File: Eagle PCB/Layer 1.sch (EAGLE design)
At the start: 247 parts, among them M1C1 33nF, M1C2 680uF, M1C3 1.0uF, M1D1 RED, M1D2 BLUE, M1J1 XT30PB-F, M1Q1 AOD482, M1R1 1k, M1R10 1k, M1R11 10k, M1R12 4.7k, M1R2 1k, M1R3 3.3k, M1R4 3.3k, M1R5 1k, M1R6 1k, M1R7 1k, M1R8 10k, M1R9 10k, M2C1 33nF, M2C2 680uF, M2C3 1.0uF, M2D1 RED, M2D2 BLUE, M2J1 XT30PB-F, M2Q1 AOD482, M2R1 1k, M2R10 1k, M2R11 10k, M2R12 4.7k, M2R2 1k, M2R3 3.3k, M2R4 3.3k, M2R5 1k, M2R6 1k, M2R7 1k, M2R8 10k, M2R9 10k, M3C1 33nF, M3C2 680uF, M3C3 1.0uF, M3D1 RED, M3D2 BLUE, M3J1 XT30PB-F, M3Q1 AOD482, M3R1 1k, M3R10 1k, M3R11 10k, M3R12 4.7k, M3R2 1k, M3R3 3.3k, M3R4 3.3k, M3R5 1k, M3R6 1k, M3R7 1k, M3R8 10k, M3R9 10k, M4C1 33nF, M4C2 680uF, M4C3 1.0uF, M4D1 RED, M4D2 BLUE, M4J1 XT30PB-F, M4Q1 AOD482, M4R1 1k, M4R10 1k, M4R11 10k, M4R12 4.7k, M4R2 1k, M4R3 3.3k, M4R4 3.3k, M4R5 1k, M4R6 1k, M4R7 1k, M4R8 10k, M4R9 10k, Q1 LIGHT_SENSORALS, Q10 LIGHT_SENSORALS, Q11 LIGHT_SENSORALS, Q12 LIGHT_SENSORALS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

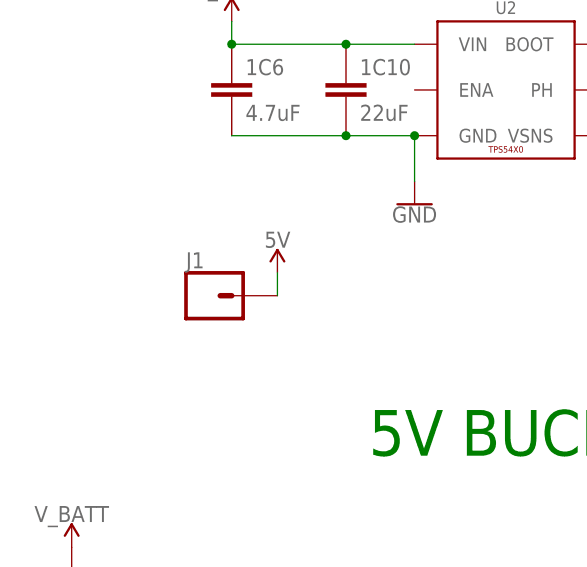
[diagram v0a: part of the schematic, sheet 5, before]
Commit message: layer 1 esc fix
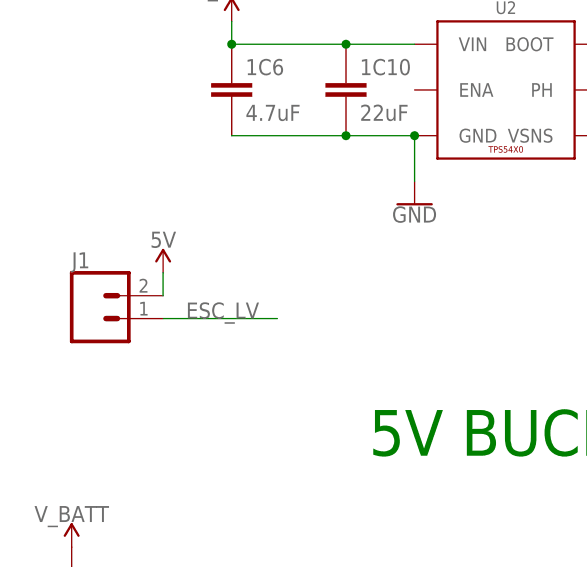
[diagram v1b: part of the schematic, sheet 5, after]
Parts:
- J1: device Connectors:CONN_01 -> Connectors:CONN_02LOCK
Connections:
- net 5V: now also J1.2; no longer J1.1
- net ESC_LV: now also J1.1
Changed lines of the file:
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@@
 <part name="SUPPLY32" library="SparkFun-PowerSymbols" deviceset="3.3V" device=""/>
 <part name="ESC_IN" library="SparkFun-Connectors" library_urn="urn:adsk.eagle:library:11010760" deviceset="CONN_03" device="LOCK" package3d_urn="urn:adsk.eagle:package:11011273/2"/>
-<part name="J1" library="Connectors" library_urn="urn:adsk.eagle:library:19813715" deviceset="CONN_01" device="" package3d_urn="urn:adsk.eagle:package:19813825/2"/>
 <part name="SUPPLY33" library="SparkFun-PowerSymbols" deviceset="5V" device=""/>
 <part name="GND39" library="SparkFun-PowerSymbols" deviceset="GND" device=""/>
+<part name="J1" library="Connectors" library_urn="urn:adsk.eagle:library:19813715" deviceset="CONN_02" device="LOCK" package3d_urn="urn:adsk.eagle:package:19813850/2"/>
 </parts>
 <sheets>
@@
 <attribute name="NAME" x="144.78" y="3.048" size="1.778" layer="95" font="vector"/>
 </instance>
-<instance part="J1" gate="G$1" x="25.4" y="55.88" smashed="yes">
-<attribute name="VALUE" x="22.86" y="51.054" size="1.778" layer="96" font="vector"/>
-<attribute name="NAME" x="22.86" y="58.928" size="1.778" layer="95" font="vector"/>
-</instance>
-<instance part="SUPPLY33" gate="G$1" x="33.02" y="58.42" smashed="yes">
-<attribute name="VALUE" x="33.02" y="61.214" size="1.778" layer="96" align="bottom-center"/>
+<instance part="SUPPLY33" gate="G$1" x="20.32" y="58.42" smashed="yes">
+<attribute name="VALUE" x="20.32" y="61.214" size="1.778" layer="96" align="bottom-center"/>
 </instance>
 <instance part="GND39" gate="1" x="165.1" y="-12.7" smashed="yes">
 <attribute name="VALUE" x="165.1" y="-12.954" size="1.778" layer="96" align="top-center"/>
 </instance>
+<instance part="J1" gate="G$1" x="12.7" y="53.34" smashed="yes">
+<attribute name="VALUE" x="10.16" y="48.514" size="1.778" layer="96" font="vector"/>
+<attribute name="NAME" x="10.16" y="58.928" size="1.778" layer="95" font="vector"/>
+</instance>
 </instances>
 <busses>
@@
 </segment>
 <segment>
-<pinref part="J1" gate="G$1" pin="1"/>
 <pinref part="SUPPLY33" gate="G$1" pin="5V"/>
-<wire x1="33.02" y1="58.42" x2="33.02" y2="55.88" width="0.1524" layer="91"/>
+<wire x1="20.32" y1="58.42" x2="20.32" y2="55.88" width="0.1524" layer="91"/>
+<pinref part="J1" gate="G$1" pin="2"/>
 </segment>
 </net>
@@
 <pinref part="Q37" gate="NMOS" pin="S"/>
 </segment>
+<segment>
+<pinref part="J1" gate="G$1" pin="1"/>
+<wire x1="20.32" y1="53.34" x2="33.02" y2="53.34" width="0.1524" layer="91"/>
+<label x="22.86" y="53.34" size="1.778" layer="95"/>
+</segment>
 </net>

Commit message: Revert "Layer 1 ESC fix"
This reverts commit 0f488ec0a57c37762cb3c7e9928ac58a828ee823.
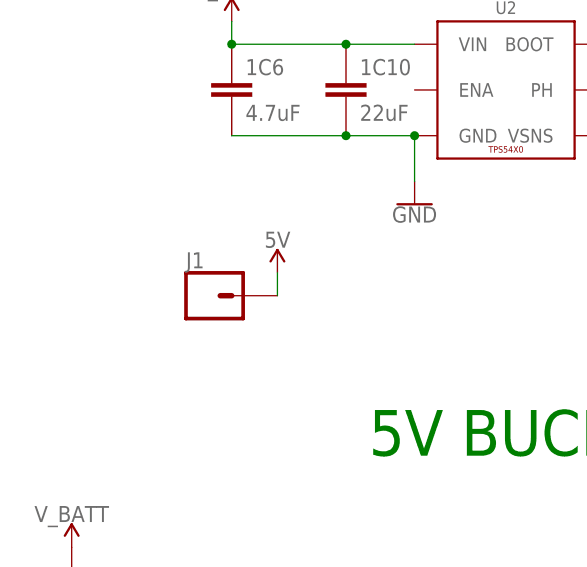
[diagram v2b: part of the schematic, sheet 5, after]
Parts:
- J1: device Connectors:CONN_02LOCK -> Connectors:CONN_01
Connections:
- net 5V: now also J1.1; no longer J1.2
- net ESC_LV: no longer J1.1
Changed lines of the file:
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@@
 <part name="SUPPLY32" library="SparkFun-PowerSymbols" deviceset="3.3V" device=""/>
 <part name="ESC_IN" library="SparkFun-Connectors" library_urn="urn:adsk.eagle:library:11010760" deviceset="CONN_03" device="LOCK" package3d_urn="urn:adsk.eagle:package:11011273/2"/>
+<part name="J1" library="Connectors" library_urn="urn:adsk.eagle:library:19813715" deviceset="CONN_01" device="" package3d_urn="urn:adsk.eagle:package:19813825/2"/>
 <part name="SUPPLY33" library="SparkFun-PowerSymbols" deviceset="5V" device=""/>
 <part name="GND39" library="SparkFun-PowerSymbols" deviceset="GND" device=""/>
-<part name="J1" library="Connectors" library_urn="urn:adsk.eagle:library:19813715" deviceset="CONN_02" device="LOCK" package3d_urn="urn:adsk.eagle:package:19813850/2"/>
 </parts>
 <sheets>
@@
 <attribute name="NAME" x="144.78" y="3.048" size="1.778" layer="95" font="vector"/>
 </instance>
-<instance part="SUPPLY33" gate="G$1" x="20.32" y="58.42" smashed="yes">
-<attribute name="VALUE" x="20.32" y="61.214" size="1.778" layer="96" align="bottom-center"/>
+<instance part="J1" gate="G$1" x="25.4" y="55.88" smashed="yes">
+<attribute name="VALUE" x="22.86" y="51.054" size="1.778" layer="96" font="vector"/>
+<attribute name="NAME" x="22.86" y="58.928" size="1.778" layer="95" font="vector"/>
+</instance>
+<instance part="SUPPLY33" gate="G$1" x="33.02" y="58.42" smashed="yes">
+<attribute name="VALUE" x="33.02" y="61.214" size="1.778" layer="96" align="bottom-center"/>
 </instance>
 <instance part="GND39" gate="1" x="165.1" y="-12.7" smashed="yes">
 <attribute name="VALUE" x="165.1" y="-12.954" size="1.778" layer="96" align="top-center"/>
 </instance>
-<instance part="J1" gate="G$1" x="12.7" y="53.34" smashed="yes">
-<attribute name="VALUE" x="10.16" y="48.514" size="1.778" layer="96" font="vector"/>
-<attribute name="NAME" x="10.16" y="58.928" size="1.778" layer="95" font="vector"/>
-</instance>
 </instances>
 <busses>
@@
 </segment>
 <segment>
+<pinref part="J1" gate="G$1" pin="1"/>
 <pinref part="SUPPLY33" gate="G$1" pin="5V"/>
-<wire x1="20.32" y1="58.42" x2="20.32" y2="55.88" width="0.1524" layer="91"/>
-<pinref part="J1" gate="G$1" pin="2"/>
+<wire x1="33.02" y1="58.42" x2="33.02" y2="55.88" width="0.1524" layer="91"/>
 </segment>
 </net>
@@
 <pinref part="Q37" gate="NMOS" pin="S"/>
 </segment>
-<segment>
-<pinref part="J1" gate="G$1" pin="1"/>
-<wire x1="20.32" y1="53.34" x2="33.02" y2="53.34" width="0.1524" layer="91"/>
-<label x="22.86" y="53.34" size="1.778" layer="95"/>
-</segment>
 </net>
